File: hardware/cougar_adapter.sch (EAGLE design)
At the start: 5 parts, among them IC1 MCP3202P

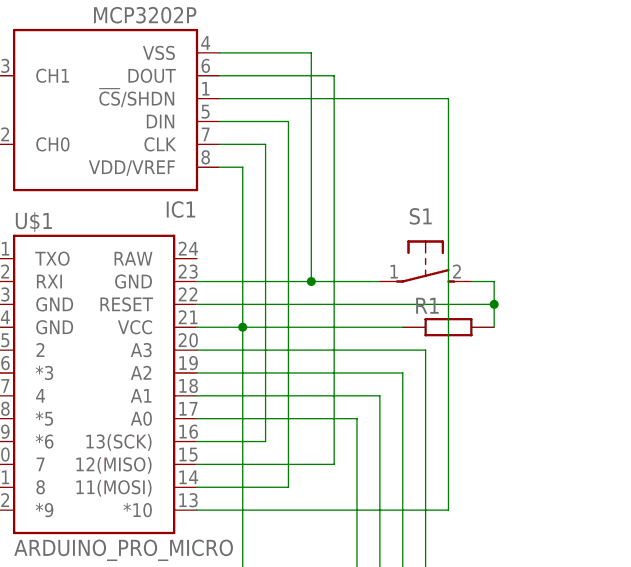
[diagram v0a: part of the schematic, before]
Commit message: Version 0.0.2: Better deadzone on the Microstick
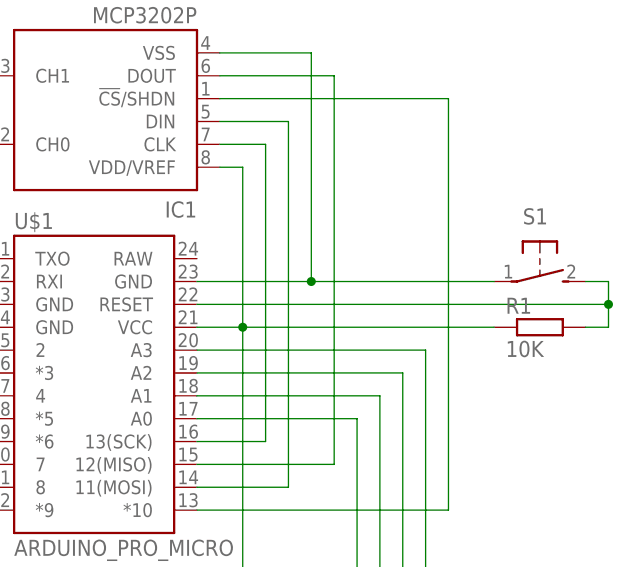
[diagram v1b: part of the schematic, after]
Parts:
- R1: value (none) -> 10K
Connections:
- net N$5 renamed 5V
- removed net N$1: IC1.VSS, S1.P, U$1.GND@2
- removed net N$10: THROTTLE.15, THROTTLE.5, U$1.GND@1
- new net GND: IC1.VSS, S1.P, THROTTLE.15, THROTTLE.5, U$1.GND@1, U$1.GND@2
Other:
- moved on the sheet: R1, S1
